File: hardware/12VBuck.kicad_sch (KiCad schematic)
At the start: 12 parts, among them U3 LMR51635XDDCR

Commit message: finished schematic except for 12v buck boost
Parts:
- removed C10: 47u, Capacitor_SMD:C_1210_3225Metric_Pad1.33x2.70mm_HandSolder, symbol Device:C_Small
- removed C11: 4.7u, Capacitor_SMD:C_0805_2012Metric_Pad1.18x1.45mm_HandSolder, symbol Device:C_Small
- removed C12: 100n, Capacitor_SMD:C_0603_1608Metric, symbol Device:C_Small
- removed C5: 100n, Capacitor_SMD:C_0805_2012Metric_Pad1.18x1.45mm_HandSolder, symbol Device:C_Small
- removed L3: 8.2u, LHRS_Passives:SRN8040-150M, symbol Device:L_Small
- removed R1: 100k, Resistor_SMD:R_0603_1608Metric, symbol Device:R_Small
- removed R4: 19.1k, Resistor_SMD:R_0603_1608Metric, symbol Device:R_Small
- removed TP10: CB, TestPoint:TestPoint_THTPad_D3.0mm_Drill1.5mm, symbol Connector:TestPoint
- removed TP9: V_in_12V, TestPoint:TestPoint_THTPad_D3.0mm_Drill1.5mm, symbol Connector:TestPoint
- removed U3: LMR51635XDDCR, LHRS_ICs:DDC0006A-MFG, symbol 2026-04-25_18-34-12:LMR51635XDDCR
- added C54: 4.7u, Capacitor_SMD:C_0805_2012Metric_Pad1.18x1.45mm_HandSolder, symbol Device:C_Small
- added C55: 100n, Capacitor_SMD:C_0805_2012Metric_Pad1.18x1.45mm_HandSolder, symbol Device:C_Small
- added C56: 100n, Capacitor_SMD:C_0603_1608Metric_Pad1.08x0.95mm_HandSolder, symbol Device:C_Small
- added C57: 47u, Capacitor_SMD:C_1210_3225Metric_Pad1.33x2.70mm_HandSolder, symbol Device:C_Small
- added L1: 8.2u, LHRS_Passives:SRN8040-150M, symbol Device:L_Small
- added R85: 100k, Resistor_SMD:R_0603_1608Metric_Pad0.98x0.95mm_HandSolder, symbol Device:R_Small
- added R86: 19.1k, Resistor_SMD:R_0603_1608Metric_Pad0.98x0.95mm_HandSolder, symbol Device:R_Small
- added TP13: FB, TestPoint:TestPoint_THTPad_D3.0mm_Drill1.5mm, symbol Connector:TestPoint
- added TP14: SW, TestPoint:TestPoint_THTPad_D3.0mm_Drill1.5mm, symbol Connector:TestPoint
- added U12: LMR51635XDDCR, LHRS_ICs:DDC0006A-MFG, symbol 2026-04-25_18-34-12:LMR51635XDDCR
- TP11: value FB -> V_in_12V
- TP12: value SW -> CB
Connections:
- net CB: now also TP12.1, C56.1, U12.6 (CB)
- net FB: now also R85.2, R86.1, TP13.1, U12.1 (FB); no longer TP11.1
- net GND: now also C54.2, C55.2, C57.2, R86.2, U12.4 (GND)
- net SW: now also C56.2, L1.1, TP14.1, U12.5 (SW); no longer TP12.1
- net V_in_12V: now also TP11.1, C54.1, C55.1, U12.2 (EN), U12.3 (VIN)
- net V_out_5V: now also C57.1, L1.2, R85.1

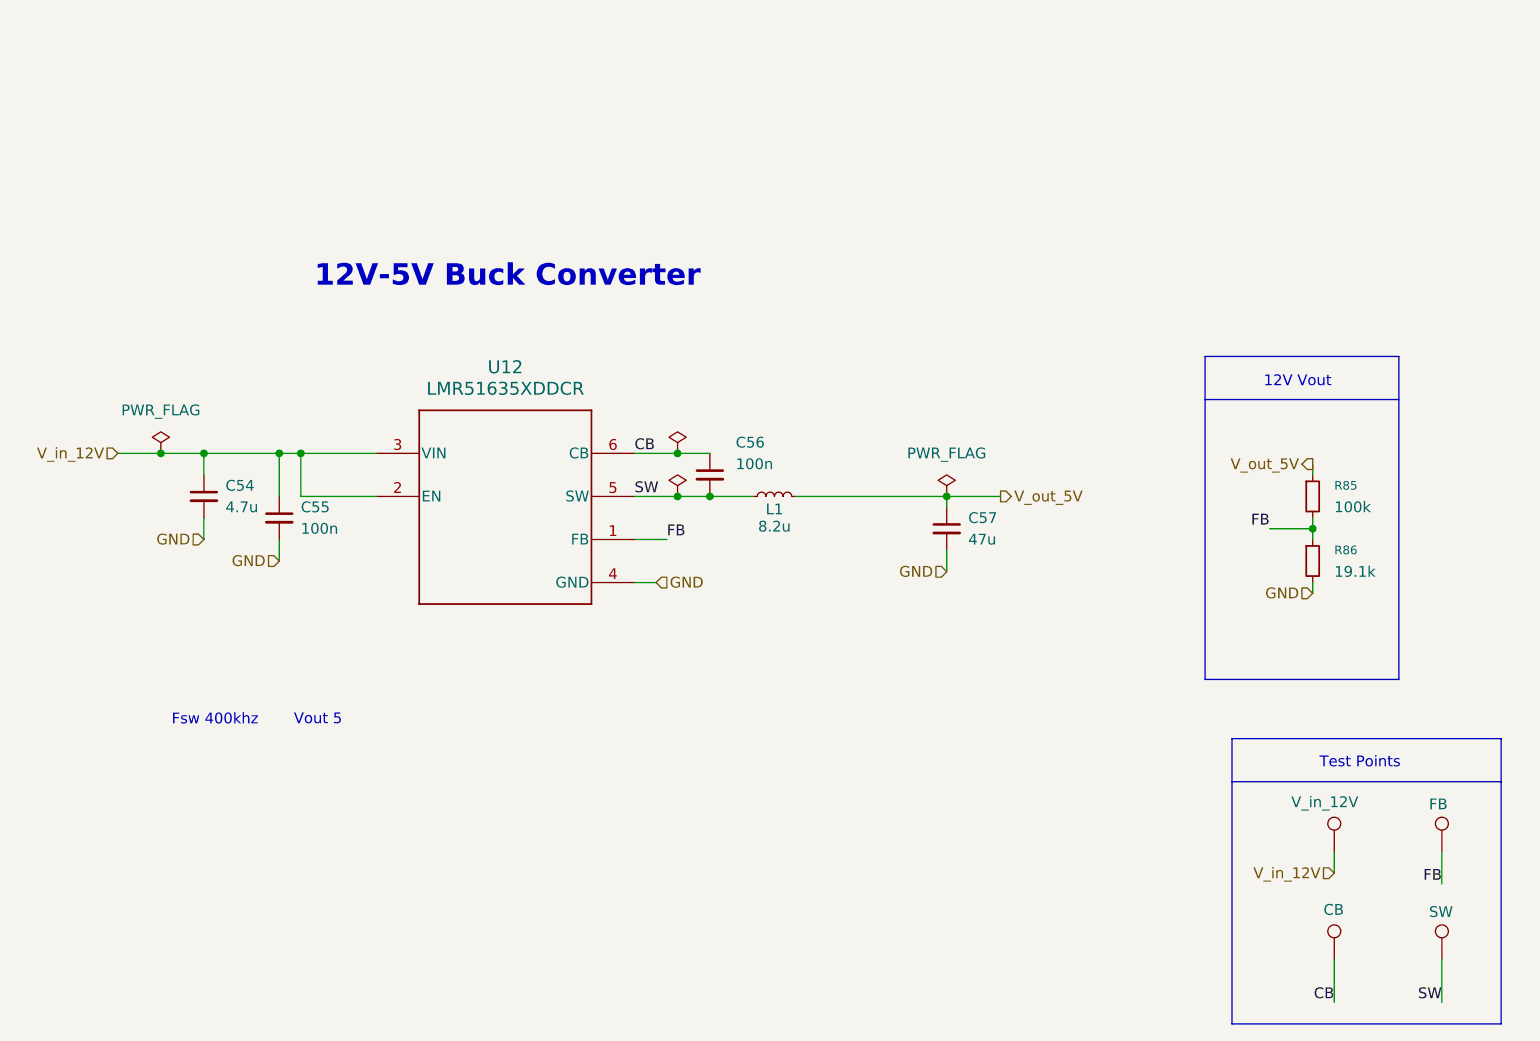
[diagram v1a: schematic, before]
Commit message: added 12V buck boost
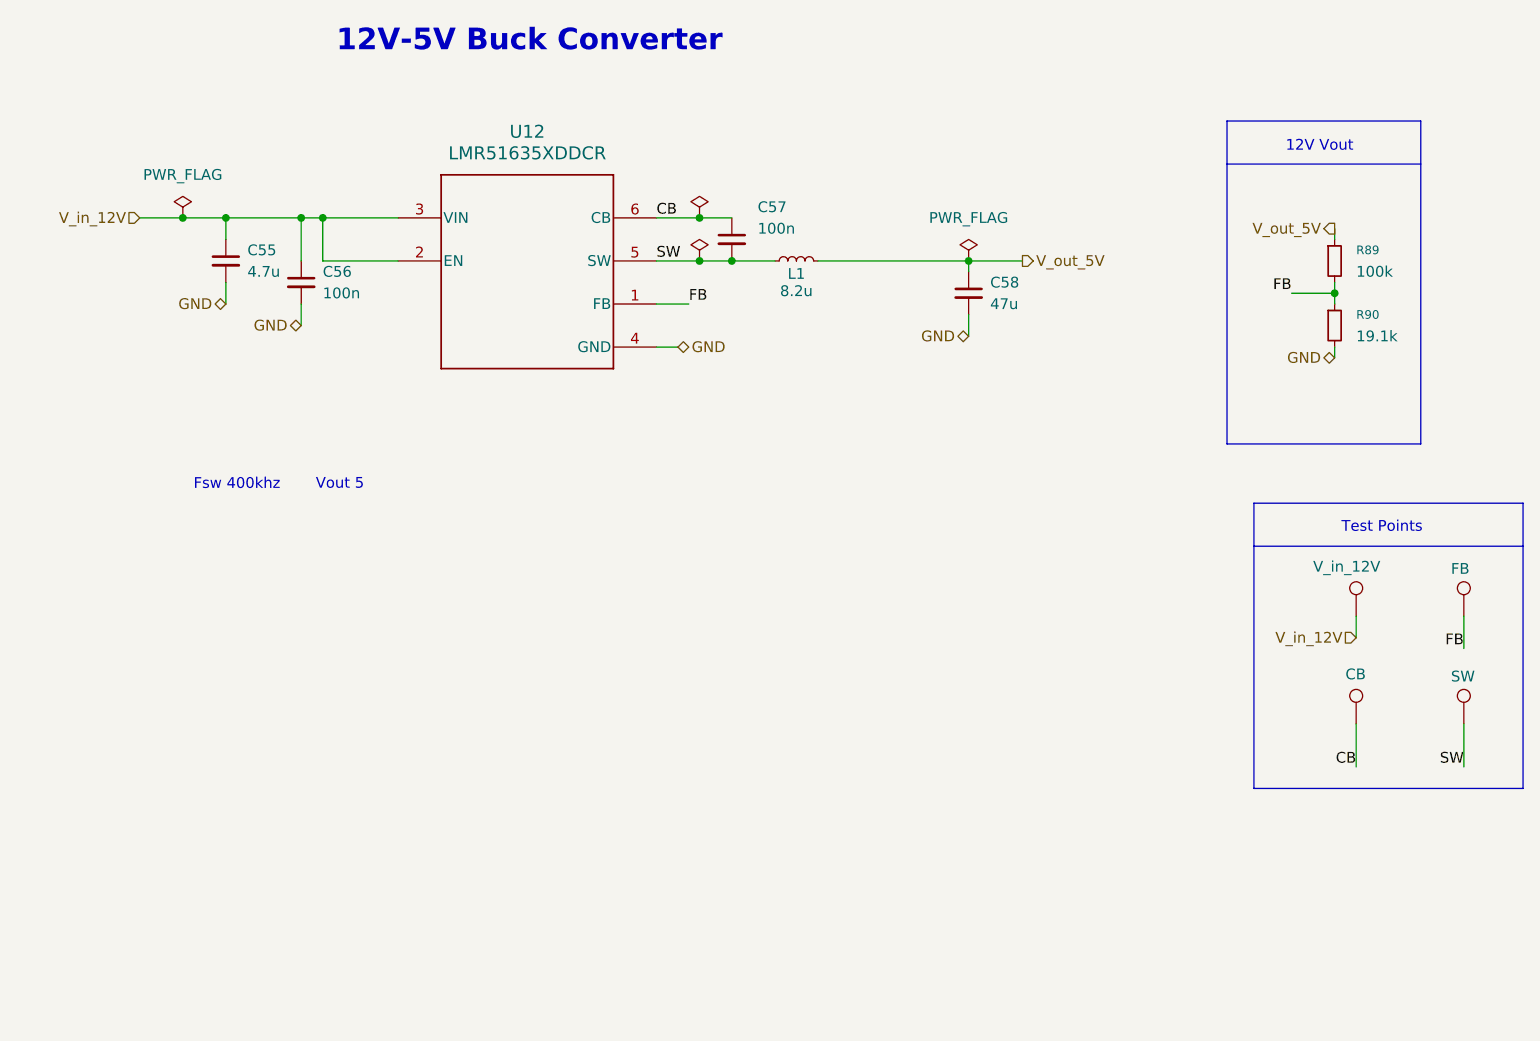
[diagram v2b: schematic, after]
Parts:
- removed C54: 4.7u, Capacitor_SMD:C_0805_2012Metric_Pad1.18x1.45mm_HandSolder, symbol Device:C_Small
- removed R85: 100k, Resistor_SMD:R_0603_1608Metric_Pad0.98x0.95mm_HandSolder, symbol Device:R_Small
- removed R86: 19.1k, Resistor_SMD:R_0603_1608Metric_Pad0.98x0.95mm_HandSolder, symbol Device:R_Small
- added C58: 47u, Capacitor_SMD:C_1210_3225Metric_Pad1.33x2.70mm_HandSolder, symbol Device:C_Small
- added R89: 100k, Resistor_SMD:R_0603_1608Metric, symbol Device:R_Small
- added R90: 19.1k, Resistor_SMD:R_0603_1608Metric, symbol Device:R_Small
- C55: value 100n -> 4.7u; LCSC P/N (none) -> C6962403; P/N MLASH168SB7104KTNA01 -> 08055D475KAT4A
- C56: LCSC P/N (none) -> C6666325
- C57: value 47u -> 100n; footprint Capacitor_SMD:C_1210_3225Metric_Pad1.33x2.70mm_HandSolder -> Capacitor_SMD:C_0603_1608Metric_Pad1.08x0.95mm_HandSolder; LCSC P/N (none) -> C6666325; P/N ZRB18AC80E476ME01L -> MLASH168SB7104KTNA01
- L1: footprint LHRS_Passives:SRN8040-150M -> LHRS_Passives:74439369082
- TP11, TP12, TP13, TP14: footprint TestPoint:TestPoint_THTPad_D3.0mm_Drill1.5mm -> TestPoint:TestPoint_Loop_D1.80mm_Drill1.0mm_Beaded
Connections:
- net CB: now also C57.1; no longer C56.1
- net FB: now also R89.2, R90.1
- net GND: now also C56.2, C58.2, R90.2; no longer C57.2
- net SW: now also C57.2; no longer C56.2
- net V_in_12V: now also C56.1
- net V_out_5V: now also C58.1, R89.1; no longer C57.1

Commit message: push gerbers and stuff
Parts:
- R89, R90: footprint Resistor_SMD:R_0603_1608Metric -> Resistor_SMD:R_0603_1608Metric_Pad0.98x0.95mm_HandSolder
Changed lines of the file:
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@@
 			)
 		)
-		(property "Footprint" "Resistor_SMD:R_0603_1608Metric"
+		(property "Footprint" "Resistor_SMD:R_0603_1608Metric_Pad0.98x0.95mm_HandSolder"
 			(at 227.3769 58.5802 0)
 			(hide yes)
@@
 			)
 		)
-		(property "Footprint" "Resistor_SMD:R_0603_1608Metric"
+		(property "Footprint" "Resistor_SMD:R_0603_1608Metric_Pad0.98x0.95mm_HandSolder"
 			(at 227.3769 66.2002 0)
 			(hide yes)
